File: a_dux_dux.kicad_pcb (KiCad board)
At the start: 2 copper layers, 119.8 x 90.9 mm, 23 parts

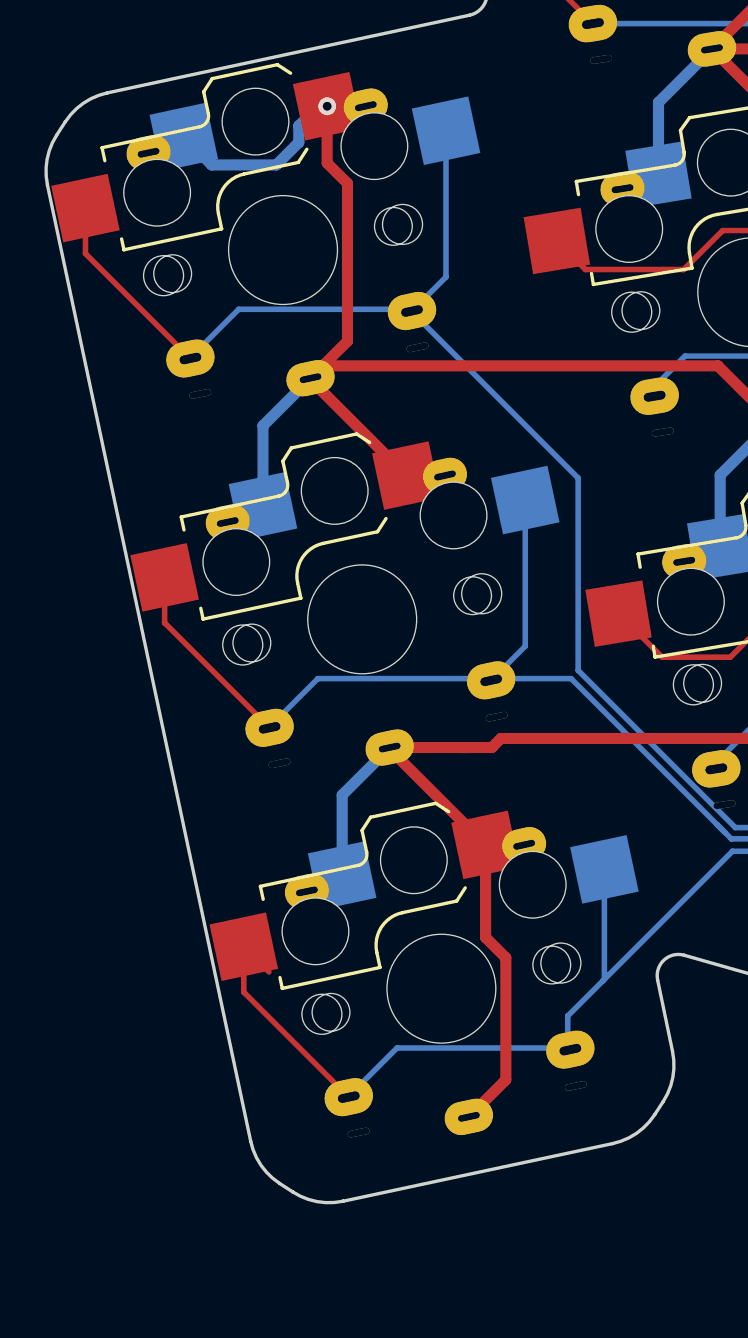
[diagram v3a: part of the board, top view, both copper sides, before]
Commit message: update hotswap gerbers
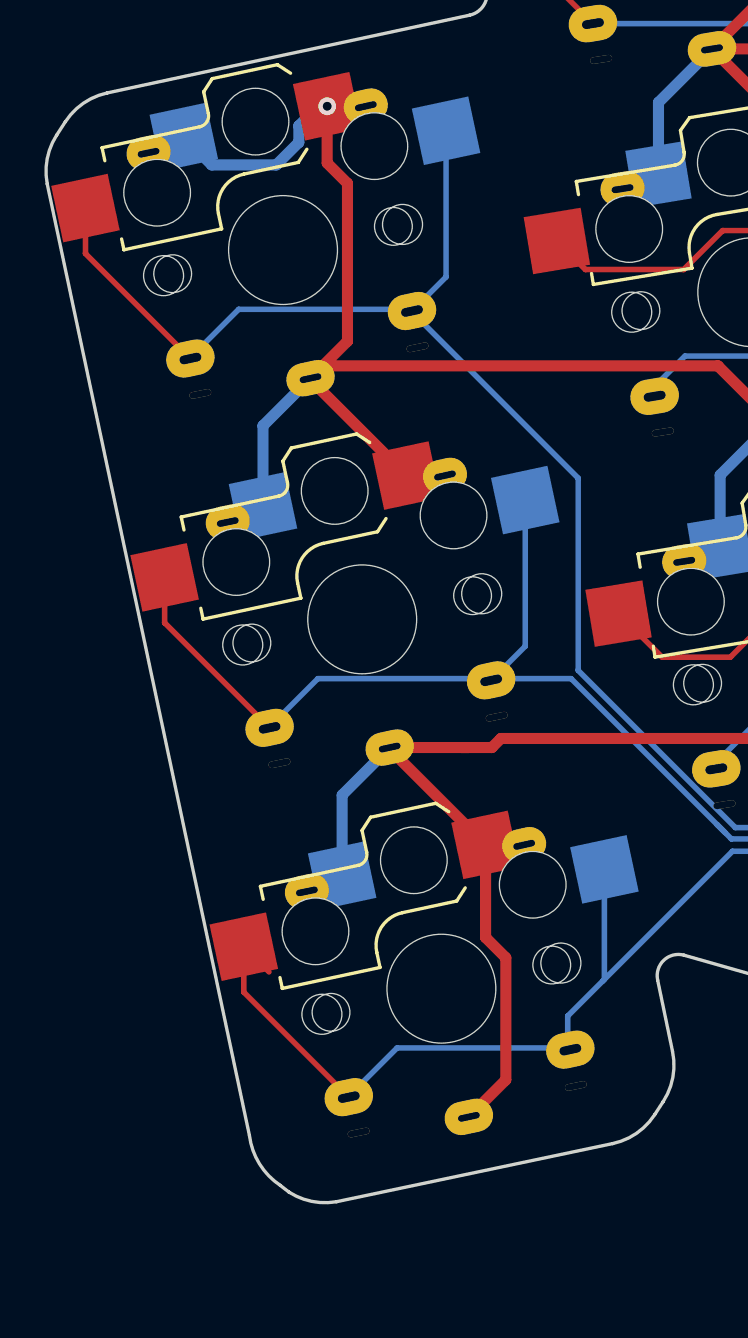
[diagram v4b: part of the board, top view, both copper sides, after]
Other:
- outline, holes or cut-outs redrawn

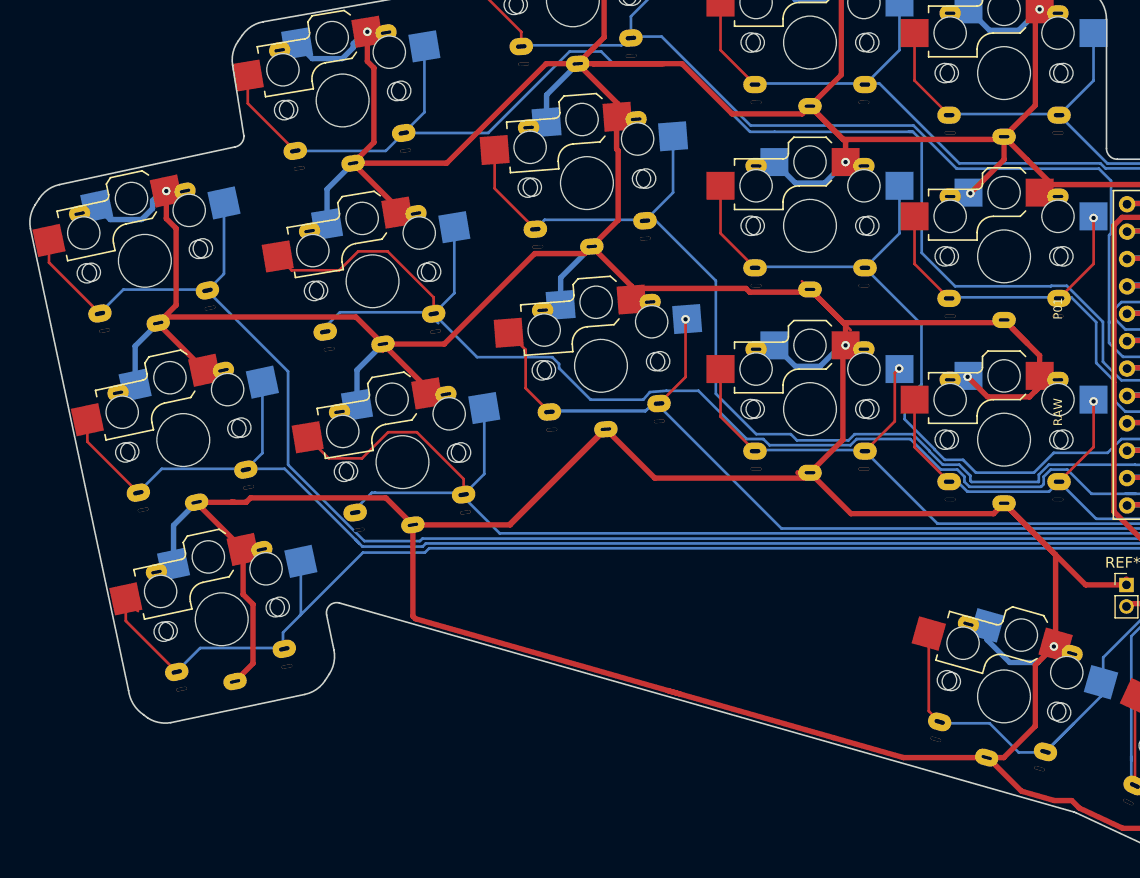
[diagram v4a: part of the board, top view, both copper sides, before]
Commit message: less pinky stagger based on initial impressions
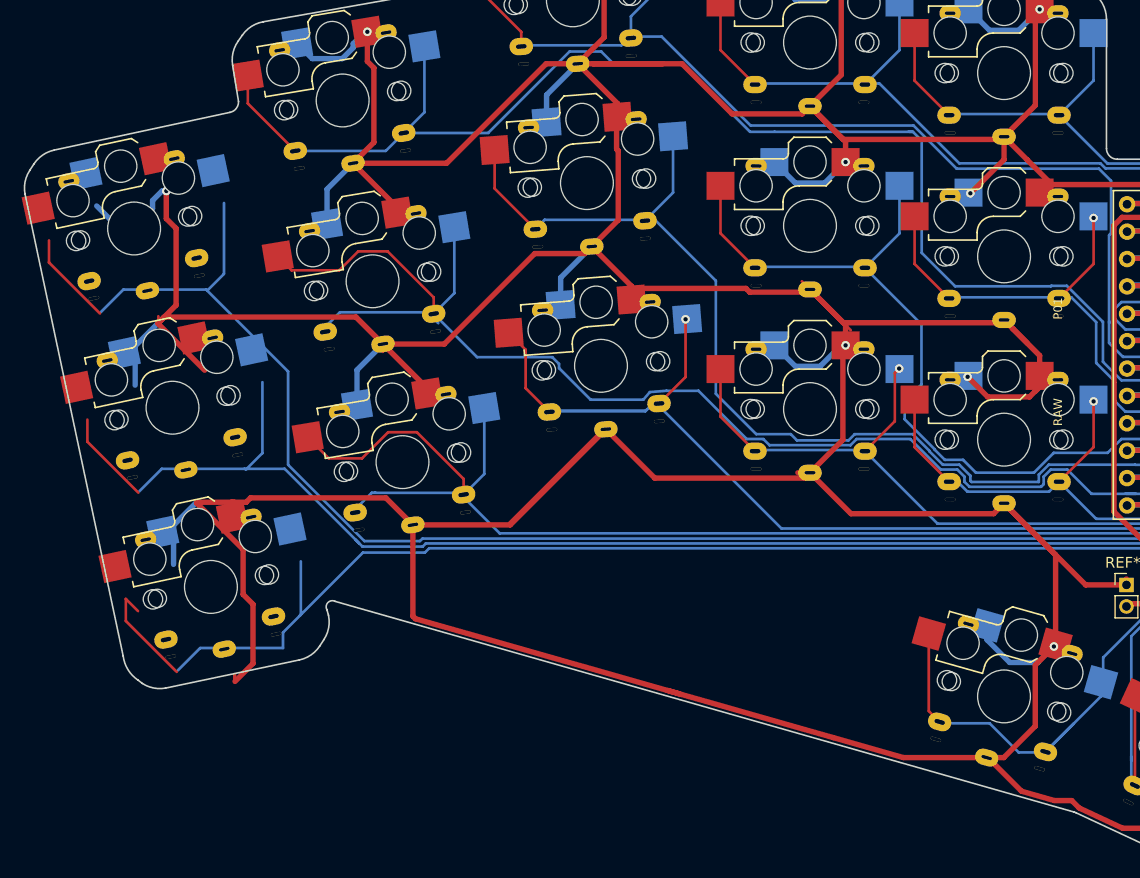
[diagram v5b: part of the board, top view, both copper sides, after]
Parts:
- moved S2 3.16 mm to (195.5, 118.5)
- moved S4 3.16 mm to (191.9, 101.9)
- moved S6 3.16 mm to (188.4, 85.3)
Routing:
- net (no net): track 124.0 -> 151.8 mm
- net P9: track 130.8 -> 120.5 mm
- net P8: track 137.0 -> 128.3 mm
- net P7: track 153.8 -> 145.1 mm
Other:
- board size 119.8 x 90.9 mm -> 120.3 x 90.9 mm
